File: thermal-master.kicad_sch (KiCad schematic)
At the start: 4 parts, among them U34 LM358-N-Q1

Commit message: syms
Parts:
- added C112, C113, C114, C115: 0.1uF, symbol Device:C
- added R267, R268: 10K, symbol Device:R
- added U58, U59: 74HC165, symbol 74xx:74HC165
- added U60, U61: 74HC595, symbol 74xx:74HC595
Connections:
- net +5V: now also C112.1, C113.1, C114.1, C115.1, R268.1, U58.16 (VCC), U59.16 (VCC), U60.10 (~{SRCLR}), U60.16 (VCC), U61.10 (~{SRCLR}), U61.16 (VCC)
- net GND: now also C112.2, C113.2, C114.2, C115.2, R267.2, U58.8 (GND), U59.8 (GND), U60.8 (GND), U61.8 (GND)
- net FEMTA_TSET renamed FEMTA_DEFAULT_TSET
- net TANK_TSET renamed TANK_DEFAULT_TSET
- new net: R267.1, U58.10 (DS)
- new net: R268.2, U60.13 (~{OE}), U61.13 (~{OE})
- new net: U60.14 (SER), U61.14 (SER)
- new net: U58.9 (Q7), U59.10 (DS)
- new net CS_HTR_STATES: U58.15 (~{CE}), U59.15 (~{CE})
- new net HTR_ON_FEMTA1: U58.11 (D0)
- new net HTR_ON_FEMTA10: U59.12 (D1)
- new net HTR_ON_FEMTA11: U59.13 (D2)
- new net HTR_ON_FEMTA12: U59.14 (D3)
- new net HTR_ON_FEMTA2: U58.12 (D1)
- new net HTR_ON_FEMTA3: U58.13 (D2)
- new net HTR_ON_FEMTA4: U58.14 (D3)
- new net HTR_ON_FEMTA5: U58.3 (D4)
- new net HTR_ON_FEMTA6: U58.4 (D5)
- new net HTR_ON_FEMTA7: U58.5 (D6)
- new net HTR_ON_FEMTA8: U58.6 (D7)
- new net HTR_ON_FEMTA9: U59.11 (D0)
- new net HTR_ON_TANK1: U59.3 (D4)
- new net HTR_ON_TANK2: U59.4 (D5)
- new net HTR_ON_TANK3: U59.5 (D6)
- new net HTR_ON_TANK4: U59.6 (D7)
- new net LOAD_HTR_STATES: U58.1 (~{PL}), U59.1 (~{PL})
- new net SPI_CLK: U58.2 (CP), U59.2 (CP)
- new net SPI_MISO: U59.9 (Q7)
- no-connect marks 0 -> 2
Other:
- sheet FEMTA Thermal Circuit 1 ports: added T_ADC; removed ADC_IN, HEATER-, THERM-
- sheet FEMTA Thermal Circuit 10 ports: added T_ADC; removed ADC_IN, HEATER-, THERM-
- sheet FEMTA Thermal Circuit 11 ports: added T_ADC; removed ADC_IN, HEATER-, THERM-
- sheet FEMTA Thermal Circuit 12 ports: added T_ADC; removed ADC_IN, HEATER-, THERM-
- sheet FEMTA Thermal Circuit 2 ports: added T_ADC; removed ADC_IN, HEATER-, THERM-
- sheet FEMTA Thermal Circuit 3 ports: added T_ADC; removed ADC_IN, HEATER-, THERM-
- sheet FEMTA Thermal Circuit 4 ports: added T_ADC; removed ADC_IN, HEATER-, THERM-
- sheet FEMTA Thermal Circuit 5 ports: added T_ADC; removed ADC_IN, HEATER-, THERM-
- sheet FEMTA Thermal Circuit 6 ports: added T_ADC; removed ADC_IN, HEATER-, THERM-
- sheet FEMTA Thermal Circuit 7 ports: added T_ADC; removed ADC_IN, HEATER-, THERM-
- sheet FEMTA Thermal Circuit 8 ports: added T_ADC; removed ADC_IN, HEATER-, THERM-
- sheet FEMTA Thermal Circuit 9 ports: added T_ADC; removed ADC_IN, HEATER-, THERM-
- sheet Tank Thermal Circuit 1 ports: added T_ADC; removed ADC_IN, HEATER-, THERM-
- sheet Tank Thermal Circuit 2 ports: added T_ADC; removed ADC_IN, HEATER-, THERM-
- sheet Tank Thermal Circuit 3 ports: added T_ADC; removed ADC_IN, HEATER-, THERM-
- sheet Tank Thermal Circuit 4 ports: added T_ADC; removed ADC_IN, HEATER-, THERM-
- note added: "It is critical that OE defaults high Else outputs may be random before microcontroller start"
- note added: "TODO: Check that this bit order makes sense"
- moved on the sheet: C91, U34C

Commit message: midnight work
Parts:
- added U62: TPS7A91, Package_DFN_QFN:Texas_S-PDSO-N10_EP1.2x2mm, symbol Regulator_Linear:TPS7A91
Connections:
- net +5V: no longer C91.1, RV1.1, RV2.1, U34.8 (V+)
- new net: U62.1 (OUT), U62.2 (OUT)
- new net: U62.10 (IN), U62.9 (IN)
- new net: U62.11 (GND), U62.4 (GND)
- new net THERMISTOR_SUP: C91.1, RV1.1, RV2.1, U34.8 (V+)
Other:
- moved on the sheet: RV1, RV2, U34A, U34B

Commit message: thermal circuit issue fixes
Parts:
- added C116, C117: 10uF, symbol Device:C
- added C118: 10nF, symbol Device:C
- added R269: 3.57K, symbol Device:R
- added R270: 1.15K, symbol Device:R
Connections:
- net +5V: now also U62.10 (IN), U62.6 (SS_CTRL), U62.7 (EN), U62.9 (IN), C117.1
- net GND: now also U62.11 (GND), U62.4 (GND), C116.2, C117.2, C118.2, R270.2
- net THERMISTOR_SUP: now also U62.1 (OUT), U62.2 (OUT), C116.1, R269.2
- net at U62.3 (FB): now also R269.1, R270.1
- net at U62.8 (NR/SS): now also C118.1
- no-connect marks 2 -> 3
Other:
- sheet Tank Thermal Circuit 1 renamed Tank Thermal Circuit
- removed sheet Tank Thermal Circuit 2
- removed sheet Tank Thermal Circuit 3
- removed sheet Tank Thermal Circuit 4
- sheet Tank Thermal Circuit: file thermal-subcircuit.kicad_sch -> thermal-subcircuit-tank.kicad_sch
- note added: "3.3V Output"
- note added: "soft start time = 0.8V*C118/100uA = 80ms"
- moved on the sheet: C91, RV1, RV2, U34A, U34B, U34C, U62

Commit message: work
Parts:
- added U28, U29: MCP3208, Package_SO:SOIC-16_3.9x9.9mm_P1.27mm, symbol Analog_ADC:MCP3208
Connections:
- net ADC_T_FEMTA1: now also U28.1 (CH0)
- net ADC_T_FEMTA10: now also U29.2 (CH1)
- net ADC_T_FEMTA11: now also U29.3 (CH2)
- net ADC_T_FEMTA12: now also U29.4 (CH3)
- net ADC_T_FEMTA2: now also U28.2 (CH1)
- net ADC_T_FEMTA3: now also U28.3 (CH2)
- net ADC_T_FEMTA4: now also U28.4 (CH3)
- net ADC_T_FEMTA5: now also U28.5 (CH4)
- net ADC_T_FEMTA6: now also U28.6 (CH5)
- net ADC_T_FEMTA7: now also U28.7 (CH6)
- net ADC_T_FEMTA8: now also U28.8 (CH7)
- net ADC_T_FEMTA9: now also U29.1 (CH0)
- net ADC_T_TANK1: now also U29.5 (CH4)
- net GND: now also U28.14 (AGND), U28.9 (DGND), U29.14 (AGND), U29.9 (DGND)
- net SPI_CLK: now also U28.13 (CLK), U29.13 (CLK)
- net SPI_MISO: now also U28.12 (Dout), U29.12 (Dout)
- net THERMISTOR_SUP: now also U28.15 (Vref), U29.15 (Vref)
- net HTR_ON_TANK2: no longer names the net of U59.4 (D5)
- net HTR_ON_TANK3: no longer names the net of U59.5 (D6)
- net HTR_ON_TANK4: no longer names the net of U59.6 (D7)
- new net +3.3V: U28.16 (Vdd), U29.16 (Vdd)
- new net ADC1_CS: U28.10 (~{CS}/SHDN)
- new net ADC2_CS: U29.10 (~{CS}/SHDN)
- new net SPI_MOSI: U28.11 (Din), U29.11 (Din)
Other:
- moved on the sheet: C116, C117, C118, R269, R270, U62

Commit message: work
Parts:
- added C108, C109, C112, C113, C114, C115, C116, C117, C118, C119: 0.1uF, symbol Device:C
- added C110, C111: 1uF, symbol Device:C
- added R251, R254: 1, symbol Device:R
- added R252, R255: 16K, symbol Device:R
- added R253, R256: 1K, symbol Device:R
- added R257, R258: 10K, symbol Device:R
- added U60, U62: SN74HCS595-Q1, femta-control:DHVQFN-16-2.5X3.5MM, symbol 74xx:74HC595
- added U61, U63: MAX4210EEUA+, symbol femta-control-custom:MAX4210
- added U64, U65: LTC2620IGN, symbol femta-control-custom:LTC2620IGN
- R236: renamed from R269; value 3.57K -> 3.16K
- U48: renamed from U60; value 74HC595 -> SN74HCS595-Q1; footprint (none) -> femta-control:DHVQFN-16-2.5X3.5MM
- U49: renamed from U58; value 74HC165 -> SN74HCS165-Q1; footprint (none) -> femta-control:DHVQFN-16-2.5X3.5MM
- U50: renamed from U59; value 74HC165 -> SN74HCS165-Q1; footprint (none) -> femta-control:DHVQFN-16-2.5X3.5MM
- U51: renamed from U61; value 74HC595 -> SN74HCS595-Q1; footprint (none) -> femta-control:DHVQFN-16-2.5X3.5MM
- renumbered C117 to C100, C118 to C101, C116 to C102, C91 to C103, C114 to C96, C112 to C97, C115 to C98, C113 to C99, R267 to R233, R268 to R234, R270 to R235, U62 to U52, U34 to U53, U28 to U54, U29 to U55
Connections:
- net +3.3V: now also C96.1, C97.1, C98.1, C99.1, U48.10 (~{SRCLR}), U48.16 (VCC), U49.16 (VCC), U50.16 (VCC), U51.10 (~{SRCLR}), U51.16 (VCC), C108.1, C109.1, C110.1, C111.1, C112.1, C115.1, C117.1, C118.1, R257.1, R258.1, U60.10 (~{SRCLR}), U60.16 (VCC), U61.4 (Vcc), U62.10 (~{SRCLR}), U62.16 (VCC), U63.4 (Vcc), U64.16 (VCC), U65.16 (VCC)
- net +5V: no longer C96.1, C97.1, C98.1, C99.1, U48.10 (~{SRCLR}), U48.16 (VCC), U49.16 (VCC), U50.16 (VCC), U51.10 (~{SRCLR}), U51.16 (VCC)
- net DAC_EN_FEMTA1: now also U48.15 (QA)
- net DAC_EN_FEMTA10: now also U51.1 (QB)
- net DAC_EN_FEMTA11: now also U51.2 (QC)
- net DAC_EN_FEMTA12: now also U51.3 (QD)
- net DAC_EN_FEMTA2: now also U48.1 (QB)
- net DAC_EN_FEMTA3: now also U48.2 (QC)
- net DAC_EN_FEMTA4: now also U48.3 (QD)
- net DAC_EN_FEMTA5: now also U48.4 (QE)
- net DAC_EN_FEMTA6: now also U48.5 (QF)
- net DAC_EN_FEMTA7: now also U48.6 (QG)
- net DAC_EN_FEMTA8: now also U48.7 (QH)
- net DAC_EN_FEMTA9: now also U51.15 (QA)
- net DAC_EN_TANK1: now also U51.4 (QE)
- net DAC_SET_FEMTA1: now also U64.2 (OUTA)
- net DAC_SET_FEMTA10: now also U65.3 (OUTB)
- net DAC_SET_FEMTA11: now also U65.4 (OUTC)
- net DAC_SET_FEMTA12: now also U65.5 (OUTD)
- net DAC_SET_FEMTA2: now also U64.3 (OUTB)
- net DAC_SET_FEMTA3: now also U64.4 (OUTC)
- net DAC_SET_FEMTA4: now also U64.5 (OUTD)
- net DAC_SET_FEMTA5: now also U64.12 (OUTE)
- net DAC_SET_FEMTA6: now also U64.13 (OUTF)
- net DAC_SET_FEMTA7: now also U64.14 (OUTG)
- net DAC_SET_FEMTA8: now also U64.15 (OUTH)
- net DAC_SET_FEMTA9: now also U65.2 (OUTA)
- net DAC_SET_TANK1: now also U65.12 (OUTE)
- net EN_FEMTA1: now also U60.15 (QA)
- net EN_FEMTA10: now also U62.1 (QB)
- net EN_FEMTA11: now also U62.2 (QC)
- net EN_FEMTA12: now also U62.3 (QD)
- net EN_FEMTA2: now also U60.1 (QB)
- net EN_FEMTA3: now also U60.2 (QC)
- net EN_FEMTA4: now also U60.3 (QD)
- net EN_FEMTA5: now also U60.4 (QE)
- net EN_FEMTA6: now also U60.5 (QF)
- net EN_FEMTA7: now also U60.6 (QG)
- net EN_FEMTA8: now also U60.7 (QH)
- net EN_FEMTA9: now also U62.15 (QA)
- net EN_TANK1: now also U62.4 (QE)
- net FEMTA_HEATER_VCC: now also R251.2, R252.1, U61.7 (RS-)
- net GND: now also U50.4 (D5), U50.5 (D6), U50.6 (D7), U55.8 (CH7), C108.2, C109.2, C110.2, C111.2, C112.2, C113.2, C114.2, C115.2, C116.2, C117.2, C118.2, C119.2, R253.2, R256.2, U60.8 (GND), U61.1 (GND), U62.8 (GND), U63.1 (GND), U64.1 (GND), U65.1 (GND)
- net SPI_CLK: now also U48.11 (SRCLK), U51.11 (SRCLK), U60.11 (SRCLK), U62.11 (SRCLK), U64.8 (SCK), U65.8 (SCK)
- net SPI_MISO: now also U64.10 (SDO), U65.10 (SDO)
- net SPI_MOSI: now also U48.14 (SER), U64.9 (SDI), U65.9 (SDI)
- net TANK_HEATER_VCC: now also R254.2, R255.1, U63.7 (RS-)
- net THERMISTOR_SUP: now also C113.1, C114.1, C116.1, C119.1, U64.6 (REF), U65.6 (REF)
- net LOAD_OUTPUTS: now reaches U48.12 (RCLK)
- net LOAD_OUTPUTS: now also U51.12 (RCLK), U60.12 (RCLK), U62.12 (RCLK)
- net EN_OUTPUTS: now reaches R234.2, U48.13 (~{OE}), U51.13 (~{OE})
- net EN_OUTPUTS: now also U60.13 (~{OE}), U62.13 (~{OE})
- net at U51.14 (SER): now also U48.9 (QH'); no longer U48.14 (SER)
- net ADC_FEMTA_PWR: now reaches U55.6 (CH5)
- net ADC_FEMTA_PWR: now also R252.2, R253.1, U61.2 (IN), U61.8 (POUT)
- net ADC_TANK_PWR: now reaches U55.7 (CH6)
- net ADC_TANK_PWR: now also R255.2, R256.1, U63.2 (IN), U63.8 (POUT)
- net at U51.9 (QH'): now also U60.14 (SER)
- new net: U63.3 (NC), U63.6 (NC)
- new net: U61.3 (NC), U61.6 (NC)
- new net: R258.2, U65.11 (~{CLR})
- new net: R257.2, U64.11 (~{CLR})
- new net: U60.9 (QH'), U62.14 (SER)
- new net +5VP: R251.1, R254.1, U61.5 (RS+), U63.5 (RS+)
- new net DAC1_CS: U64.7 (~{CS}/LD), U65.7 (~{CS}/LD)
- no-connect marks 3 -> 12
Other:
- note added: "3.0V Output"
- note added: "CHECK BIT ORDERS"
- note added: "soft start time = 0.8V*C(ss)/100uA = 80ms"
- note removed: "3.3V Output"
- note removed: "soft start time = 0.8V*C118/100uA = 80ms"
- moved on the sheet: C100, C101, C102, C103, C96, C97, C98, C99, R233, R234, R235, R236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

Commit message: work
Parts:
- R251, R254: value 1 -> 100m
- R252, R255: value 16K -> 20K
- R253, R256: value 1K -> 30K
- U61, U63: value MAX4210EEUA+ -> MAX4210DEUA+
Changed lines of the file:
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@@
 			)
 		)
-		(property "Value" "1K"
+		(property "Value" "30K"
 			(at 171.45 86.36 90)
 			(effects
@@
 			)
 		)
-		(property "Value" "1"
+		(property "Value" "100m"
 			(at 146.05 74.93 90)
 			(effects
@@
 			)
 		)
-		(property "Value" "MAX4210EEUA+"
+		(property "Value" "MAX4210DEUA+"
 			(at 151.13 81.534 0)
 			(do_not_autoplace yes)
@@
 			)
 		)
-		(property "Value" "16K"
+		(property "Value" "20K"
 			(at 170.18 26.67 90)
 			(effects
@@
 			)
 		)
-		(property "Value" "1K"
+		(property "Value" "30K"
 			(at 170.18 34.29 90)
 			(effects
@@
 			)
 		)
-		(property "Value" "MAX4210EEUA+"
+		(property "Value" "MAX4210DEUA+"
 			(at 149.86 29.464 0)
 			(do_not_autoplace yes)
@@
 			)
 		)
-		(property "Value" "1"
+		(property "Value" "100m"
 			(at 144.78 22.86 90)
 			(effects
@@
 			)
 		)
-		(property "Value" "16K"
+		(property "Value" "20K"
 			(at 171.45 78.74 90)
 			(effects

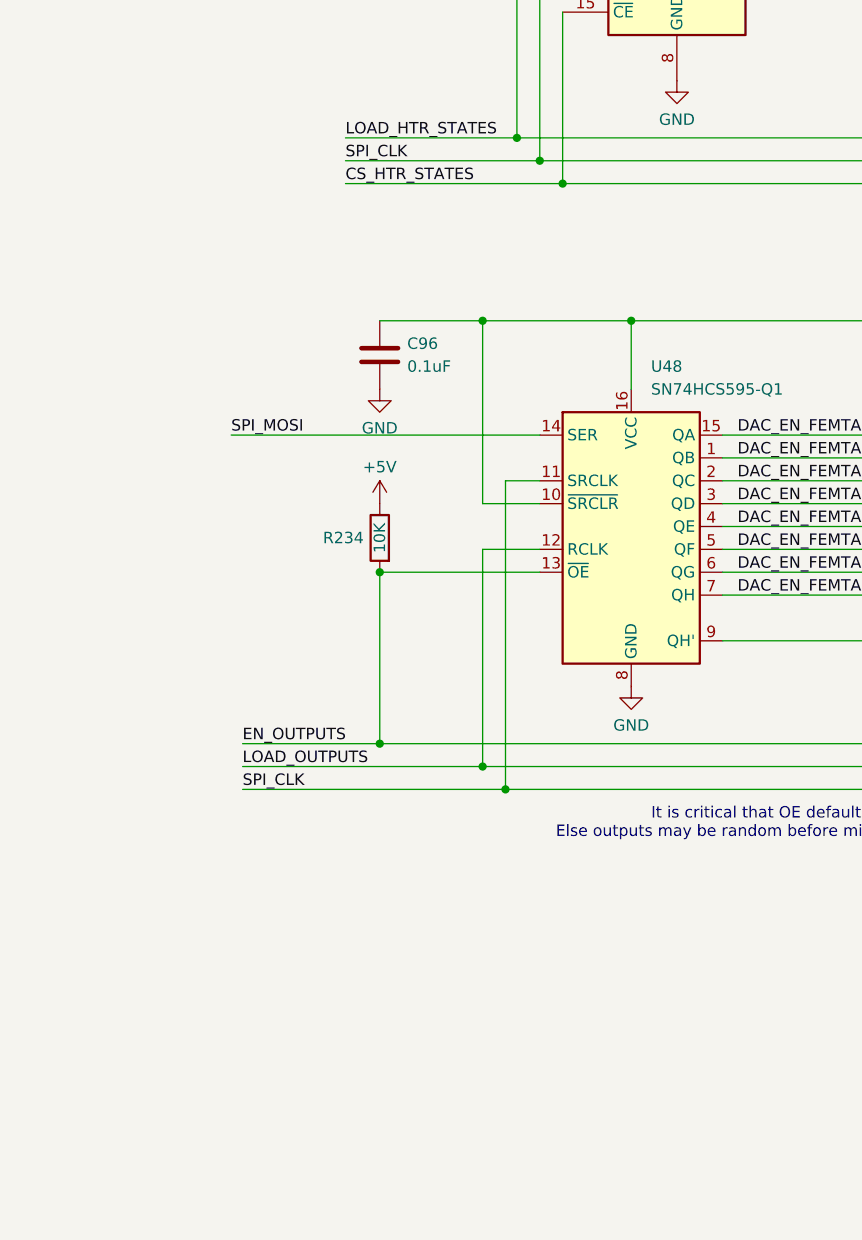
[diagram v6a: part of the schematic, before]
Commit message: chip select for 595s
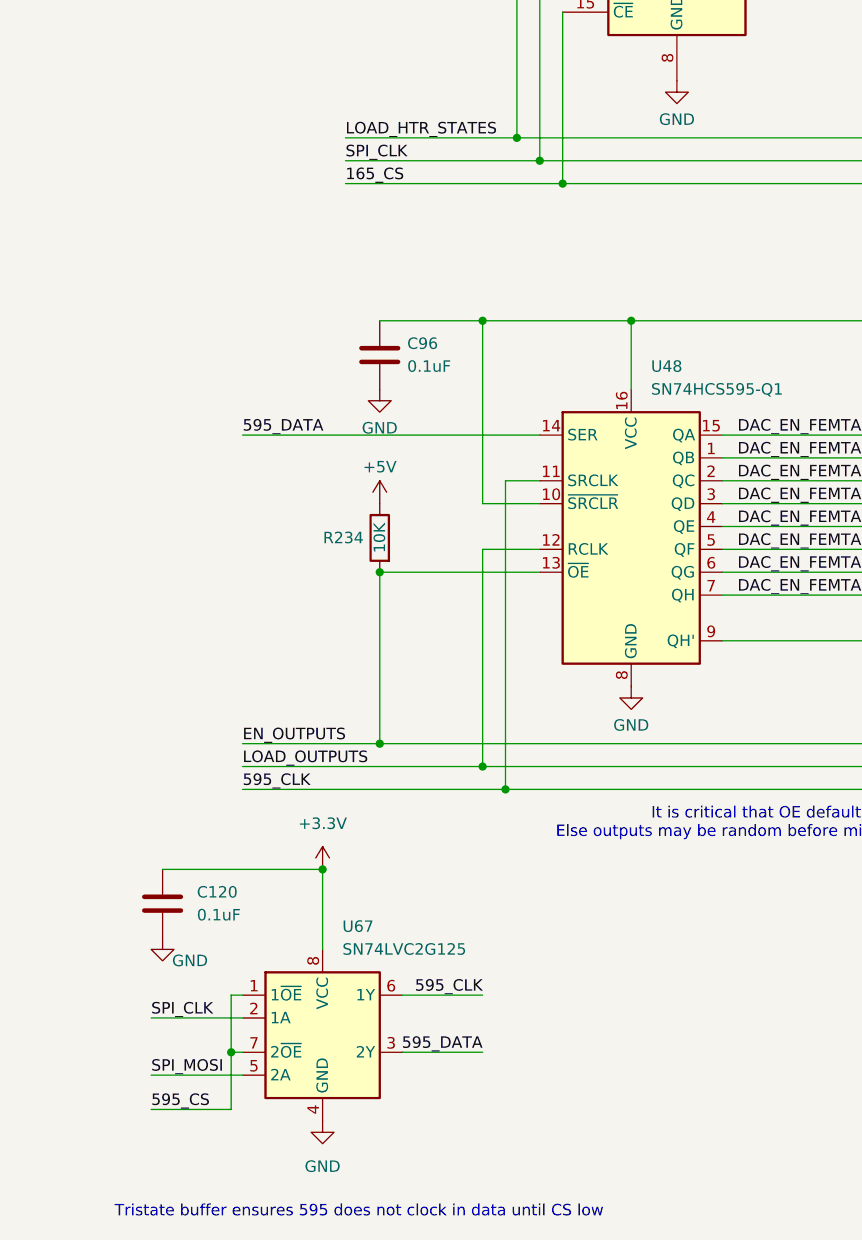
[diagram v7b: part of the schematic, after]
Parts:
- added C120: 0.1uF, symbol Device:C
- added U67: SN74LVC2G125, Package_SO:VSSOP-8_2.4x2.1mm_P0.5mm, symbol femta-control-custom:SN74LVC2G125DCU-Q1
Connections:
- net +3.3V: now also C120.1, U67.8 (VCC)
- net GND: now also C120.2, U67.4 (GND)
- net SPI_CLK: now also U67.2 (1A); no longer U48.11 (SRCLK), U51.11 (SRCLK), U60.11 (SRCLK), U62.11 (SRCLK)
- net SPI_MOSI: now also U67.5 (2A); no longer U48.14 (SER)
- net CS_HTR_STATES renamed 165_CS
- new net 595_CLK: U48.11 (SRCLK), U51.11 (SRCLK), U60.11 (SRCLK), U62.11 (SRCLK), U67.6 (1Y)
- new net 595_CS: U67.1 (1~{OE}), U67.7 (2~{OE})
- new net 595_DATA: U48.14 (SER), U67.3 (2Y)
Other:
- note added: "Tristate buffer ensures 595 does not clock in data until CS low"

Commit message: consolidate heaters
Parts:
- removed C108, C109, C118, C119, C99: 0.1uF, symbol Device:C
- removed C110, C111: 1uF, symbol Device:C
- removed R233, R258: 10K, symbol Device:R
- removed R251, R254: 100m, symbol Device:R
- removed R252, R255: 20K, symbol Device:R
- removed R253, R256: 30K, symbol Device:R
- removed U50: SN74HCS165-Q1, femta-control:DHVQFN-16-2.5X3.5MM, symbol 74xx:74HC165
- removed U60, U62: SN74HCS595-Q1, femta-control:DHVQFN-16-2.5X3.5MM, symbol 74xx:74HC595
- removed U61, U63: MAX4210DEUA+, symbol femta-control-custom:MAX4210
- removed U65: LTC2620IGN, symbol femta-control-custom:LTC2620IGN
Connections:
- net ADC_T_FEMTA7 is gone; now on net ADC_T_TANK1: U54.7 (CH6)
- net ADC_T_FEMTA8 is gone; now on net GND: U54.8 (CH7)
- net DAC_EN_FEMTA10 is gone; now on net EN_FEMTA2: U51.1 (QB)
- net DAC_EN_FEMTA11 is gone; now on net EN_FEMTA3: U51.2 (QC)
- net DAC_EN_FEMTA12 is gone; now on net EN_FEMTA4: U51.3 (QD)
- net DAC_EN_FEMTA7 is gone; now on net DAC_EN_TANK1: U48.6 (QG)
- net DAC_EN_FEMTA9 is gone; now on net EN_FEMTA1: U51.15 (QA)
- net DAC_SET_FEMTA7 is gone; now on net DAC_SET_TANK1: U64.14 (OUTG)
- net HTR_ON_FEMTA7 is gone; now on net HTR_ON_TANK1: U49.5 (D6)
- net HTR_ON_FEMTA8 is gone; now on net GND: U49.6 (D7)
- net ADC_T_TANK1: no longer U55.5 (CH4)
- net DAC_EN_TANK1: no longer U51.4 (QE)
- net EN_FEMTA5: now also U51.4 (QE)
- net EN_FEMTA6: now also U51.5 (QF)
- net EN_TANK1: now also U51.6 (QG)
- net GND: now also U49.10 (DS)
- net SPI_MISO: now also U49.9 (Q7)
- net ADC_FEMTA_PWR renamed ADC_P_FEMTA6
- net ADC_TANK_PWR renamed ADC_P_TANK1
- net ADC_T_FEMTA10 renamed ADC_P_FEMTA2
- net ADC_T_FEMTA11 renamed ADC_P_FEMTA3
- net ADC_T_FEMTA12 renamed ADC_P_FEMTA4
- net ADC_T_FEMTA9 renamed ADC_P_FEMTA1
- net DAC_EN_FEMTA8: no longer names the net of U48.7 (QH)
- net DAC_SET_FEMTA8: no longer names the net of U64.15 (OUTH)
- new net ADC_P_FEMTA5: U55.5 (CH4)
- no-connect marks 12 -> 6
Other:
- removed sheet FEMTA Thermal Circuit 10
- removed sheet FEMTA Thermal Circuit 11
- removed sheet FEMTA Thermal Circuit 12
- removed sheet FEMTA Thermal Circuit 7
- removed sheet FEMTA Thermal Circuit 8
- removed sheet FEMTA Thermal Circuit 9
- sheet FEMTA Thermal Circuit 1 ports: added ADC_PWR; removed HEATER_VCC
- sheet FEMTA Thermal Circuit 2 ports: added ADC_PWR; removed HEATER_VCC
- sheet FEMTA Thermal Circuit 3 ports: added ADC_PWR; removed HEATER_VCC
- sheet FEMTA Thermal Circuit 4 ports: added ADC_PWR; removed HEATER_VCC
- sheet FEMTA Thermal Circuit 5 ports: added ADC_PWR; removed HEATER_VCC
- sheet FEMTA Thermal Circuit 6 ports: added ADC_PWR; removed HEATER_VCC
- sheet Tank Thermal Circuit ports: added ADC_PWR; removed HEATER_VCC
- note removed: "CHECK BIT ORDERS"
- note removed: "TODO: Check that this bit order makes sense"
- moved on the sheet: C100, C101, C102, C103, C112, C113, C114, C115, C116, C117, C120, C96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
